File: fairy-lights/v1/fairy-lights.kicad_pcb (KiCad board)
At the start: 2 copper layers, 60 x 40 mm, 14 parts, among them J1 Conn_01x03_Male, J2 Screw_Terminal_01x02, J3 Conn_01x02_Pin, Q1 BSS138, U1 WeMos_D1_mini

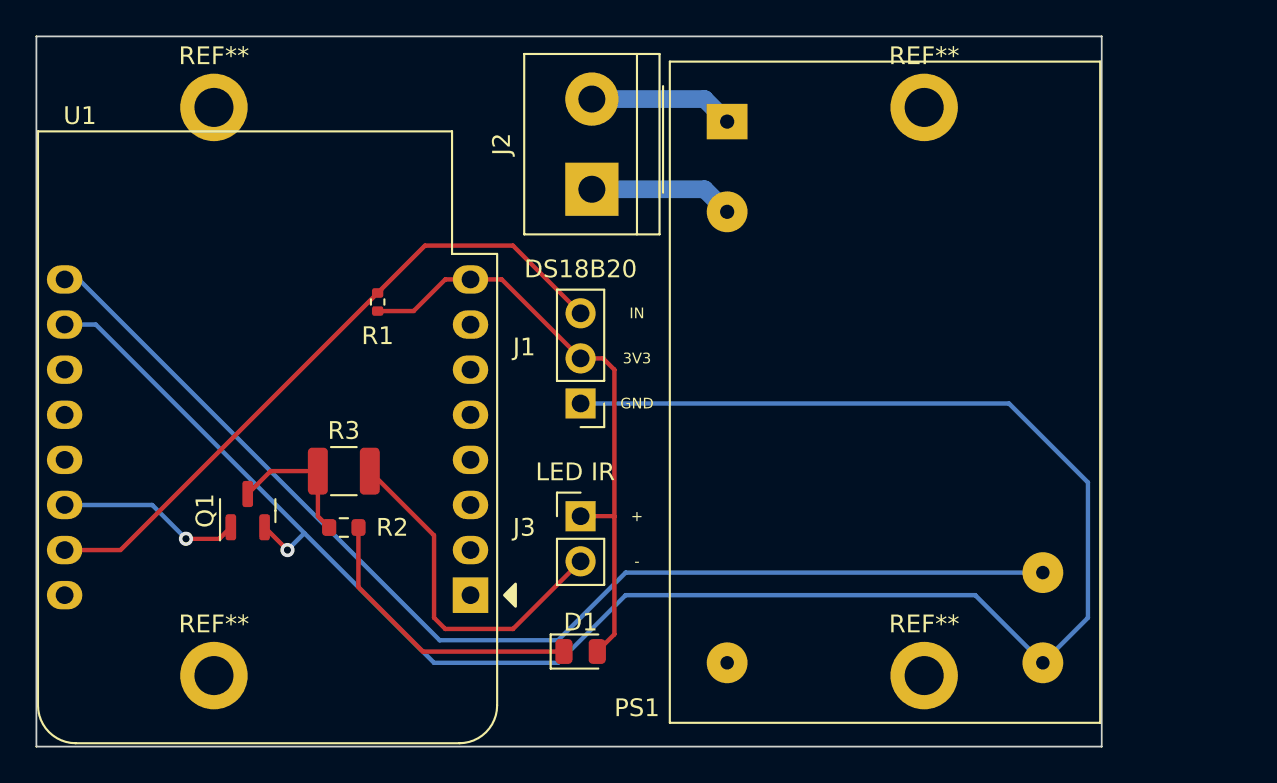
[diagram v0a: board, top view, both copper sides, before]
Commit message: finish schematic + footprints
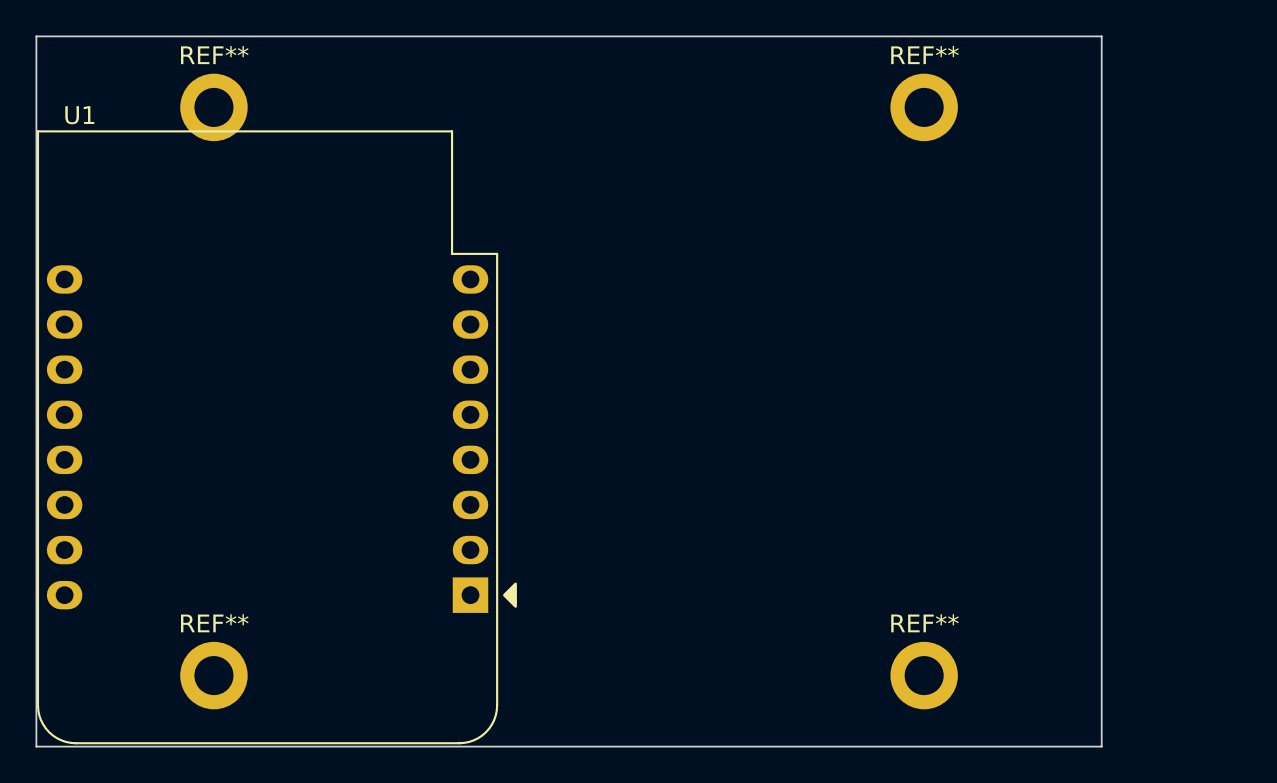
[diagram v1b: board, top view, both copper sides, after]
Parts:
- removed D1: LED, Diode_SMD:D_0805_2012Metric
- removed J1: Conn_01x03_Male, Connector_PinHeader_2.54mm:PinHeader_1x03_P2.54mm_Vertical
- removed J2: Screw_Terminal_01x02, TerminalBlock:TerminalBlock_bornier-2_P5.08mm
- removed J3: Conn_01x02_Pin, Connector_PinHeader_2.54mm:PinHeader_1x02_P2.54mm_Vertical
- removed PS1: Alim RS PRO 5V 1A, Converter_ACDC:Converter_ACDC_MeanWell_IRM-03-xx_THT
- removed Q1: BSS138, Package_TO_SOT_SMD:SOT-23
- removed R1: 4.7KΩ, Resistor_SMD:R_0402_1005Metric
- removed R2: 1KΩ, Resistor_SMD:R_0603_1608Metric
- removed R3: 18Ω/0.5W, Resistor_SMD:R_1210_3225Metric
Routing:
- net GND: track 110.9 -> 0.00 mm, vias 1 -> 0
- net +5V: track 65.1 -> 0.80 mm
- net Net-(J1-Pin_3): track 37.7 -> 0.00 mm
- net +3V3: track 34.4 -> 0.00 mm
- net Net-(J3-Pin_2): track 19.8 -> 0.00 mm
- net Net-(D1-K): track 16.4 -> 0.00 mm
- net Net-(Q1-G): track 10.4 -> 0.00 mm, vias 1 -> 0
- net NEUT: track 8.15 -> 0.00 mm
- net LINE: track 8.15 -> 0.00 mm
- net Net-(Q1-D): track 7.92 -> 0.00 mm
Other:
- board text removed: "+"
- board text removed: "-"
- board text removed: "3V3"
- board text removed: "DS18B20"
- board text removed: "GND"
- board text removed: "IN"
- board text removed: "LED IR"

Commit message: placement
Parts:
- added HS1: Heatsink, Heatsink:Heatsink_Fischer_SK104-STC-STIC_35x13mm_2xDrill2.5mm, F.Cu at (124.8, 67.3)
- added J2: Screw_Terminal_01x02, TerminalBlock:TerminalBlock_bornier-2_P5.08mm, F.Cu at (139.1, 69.8)
- added J4: Screw_Terminal_01x03, TerminalBlock:TerminalBlock_bornier-3_P5.08mm, F.Cu at (146.7, 59.7)
- added Q1: IRLZ44N, Package_TO_SOT_THT:TO-220-3_Vertical, F.Cu at (121.3, 64.8)
- added R1: 10KΩ, Resistor_THT:R_Axial_DIN0207_L6.3mm_D2.5mm_P15.24mm_Horizontal, F.Cu at (95.9, 54.6)
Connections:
- U1 pad 8: +3V3 -> unconnected-(U1-3V3-Pad8)

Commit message: wip routing
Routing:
- net GND: track 0.00 -> 72.8 mm
- net Net-(J4-Pin_3): track 0.00 -> 18.4 mm
- net +5V: track 0.80 -> 14.1 mm
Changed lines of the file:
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@@
   (gr_rect locked (start 90 46) (end 150 86)
     (stroke (width 0.1) (type default)) (fill none) (layer "Edge.Cuts"))
+  (segment (start 128.905 74.93) (end 123.825 69.85) (width 1) (layer "B.Cu") (net 1))
+  (segment (start 139.065 74.93) (end 128.905 74.93) (width 1) (layer "B.Cu") (net 1))
+  (segment (start 118.745 80.01) (end 109.37 80.01) (width 0.25) (layer "B.Cu") (net 1))
+  (segment (start 109.37 80.01) (end 91.59 62.23) (width 0.25) (layer "B.Cu") (net 1))
+  (segment (start 121.285 77.47) (end 118.745 80.01) (width 0.25) (layer "B.Cu") (net 1))
+  (segment (start 123.825 69.85) (end 121.285 69.85) (width 1) (layer "B.Cu") (net 1))
+  (segment (start 144.145 69.85) (end 139.065 74.93) (width 1) (layer "B.Cu") (net 1))
+  (segment (start 121.285 69.85) (end 121.285 77.47) (width 0.25) (layer "B.Cu") (net 1))
+  (segment (start 146.685 59.69) (end 139.065 67.31) (width 1) (layer "B.Cu") (net 2))
   (segment (start 92.3925 59.69) (end 91.59 59.69) (width 0.25) (layer "B.Cu") (net 2))
+  (segment (start 139.065 67.31) (end 139.065 69.85) (width 1) (layer "B.Cu") (net 2))
+  (segment (start 121.285 67.31) (end 128.905 67.31) (width 1) (layer "B.Cu") (net 16))
+  (segment (start 128.905 67.31) (end 136.525 59.69) (width 1) (layer "B.Cu") (net 16))
   (group "" (id d3af2464-7c72-4396-9bd6-7c833b8b6ea2)
     (members

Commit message: routing
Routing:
- net +5V: track 14.1 -> 76.8 mm
- net Net-(J4-Pin_2): track 0.00 -> 62.6 mm
- net Net-(Q1-G): track 0.00 -> 49.6 mm
- net GND: track 72.8 -> 92.9 mm
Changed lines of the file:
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@@
   (gr_rect locked (start 90 46) (end 150 86)
     (stroke (width 0.1) (type default)) (fill none) (layer "Edge.Cuts"))
+  (segment (start 111.125 54.61) (end 112.25637 54.61) (width 0.25) (layer "B.Cu") (net 1))
+  (segment (start 118.745 67.31) (end 121.285 69.85) (width 0.25) (layer "B.Cu") (net 1))
   (segment (start 128.905 74.93) (end 123.825 69.85) (width 1) (layer "B.Cu") (net 1))
   (segment (start 139.065 74.93) (end 128.905 74.93) (width 1) (layer "B.Cu") (net 1))
@@
   (segment (start 109.37 80.01) (end 91.59 62.23) (width 0.25) (layer "B.Cu") (net 1))
   (segment (start 121.285 77.47) (end 118.745 80.01) (width 0.25) (layer "B.Cu") (net 1))
+  (segment (start 112.25637 54.61) (end 118.745 61.09863) (width 0.25) (layer "B.Cu") (net 1))
   (segment (start 123.825 69.85) (end 121.285 69.85) (width 1) (layer "B.Cu") (net 1))
   (segment (start 144.145 69.85) (end 139.065 74.93) (width 1) (layer "B.Cu") (net 1))
+  (segment (start 118.745 61.09863) (end 118.745 67.31) (width 0.25) (layer "B.Cu") (net 1))
   (segment (start 121.285 69.85) (end 121.285 77.47) (width 0.25) (layer "B.Cu") (net 1))
   (segment (start 146.685 59.69) (end 139.065 67.31) (width 1) (layer "B.Cu") (net 2))
-  (segment (start 92.3925 59.69) (end 91.59 59.69) (width 0.25) (layer "B.Cu") (net 2))
+  (segment (start 100.965 59.69) (end 111.125 49.53) (width 0.25) (layer "B.Cu") (net 2))
+  (segment (start 141.605 54.61) (end 146.685 59.69) (width 0.25) (layer "B.Cu") (net 2))
+  (segment (start 111.125 49.53) (end 133.985 49.53) (width 0.25) (layer "B.Cu") (net 2))
+  (segment (start 91.59 59.69) (end 100.965 59.69) (width 0.25) (layer "B.Cu") (net 2))
+  (segment (start 139.065 54.61) (end 141.605 54.61) (width 0.25) (layer "B.Cu") (net 2))
+  (segment (start 133.985 49.53) (end 139.065 54.61) (width 0.25) (layer "B.Cu") (net 2))
   (segment (start 139.065 67.31) (end 139.065 69.85) (width 1) (layer "B.Cu") (net 2))
+  (segment (start 95.885 68.095) (end 95.885 54.61) (width 0.25) (layer "F.Cu") (net 3))
+  (segment (start 121.285 64.77) (end 121.285 62.23) (width 0.25) (layer "F.Cu") (net 3))
+  (segment (start 91.59 72.39) (end 95.885 68.095) (width 0.25) (layer "F.Cu") (net 3))
+  (segment (start 121.285 62.23) (end 116.205 57.15) (width 0.25) (layer "F.Cu") (net 3))
+  (segment (start 116.205 57.15) (end 95.885 57.15) (width 0.25) (layer "F.Cu") (net 3))
+  (segment (start 108.585 82.55) (end 113.665 82.55) (width 0.25) (layer "F.Cu") (net 15))
+  (segment (start 113.665 82.55) (end 133.985 62.23) (width 0.25) (layer "F.Cu") (net 15))
+  (segment (start 91.59 74.93) (end 100.965 74.93) (width 0.25) (layer "F.Cu") (net 15))
+  (segment (start 100.965 74.93) (end 108.585 82.55) (width 0.25) (layer "F.Cu") (net 15))
+  (segment (start 139.065 62.23) (end 141.605 59.69) (width 0.25) (layer "F.Cu") (net 15))
+  (segment (start 133.985 62.23) (end 139.065 62.23) (width 0.25) (layer "F.Cu") (net 15))
   (segment (start 121.285 67.31) (end 128.905 67.31) (width 1) (layer "B.Cu") (net 16))
   (segment (start 128.905 67.31) (end 136.525 59.69) (width 1) (layer "B.Cu") (net 16))

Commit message: routing + sign
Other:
- board text added: "Éléonore et Papa"

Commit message: wiring
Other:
- board text added: "+"
- board text added: "-"
- board text added: ". +"
- board text added: "D"
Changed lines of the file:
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@@
     (property "ki_keywords" "screw terminal")
     (attr through_hole)
-    (fp_text reference "J4" (at 2.54 5.08) (layer "F.SilkS")
+    (fp_text reference "J4" (at 13.97 1.27) (layer "F.SilkS")
         (effects (font (size 1 1) (thickness 0.15)))
     )
@@
   (gr_rect locked (start 90 46) (end 150 86)
     (stroke (width 0.1) (type default)) (fill none) (layer "Edge.Cuts"))
+  (gr_text " .\n+" (at 145.415 55.88) (layer "F.SilkS")
+    (effects (font (size 1.5 1.5) (thickness 0.3) bold) (justify left bottom))
+  )
+  (gr_text "D" (at 140.335 55.88) (layer "F.SilkS")
+    (effects (font (size 1.5 1.5) (thickness 0.3) bold) (justify left bottom))
+  )
+  (gr_text "-" (at 142.875 75.565) (layer "F.SilkS")
+    (effects (font (size 1.5 1.5) (thickness 0.3) bold) (justify left bottom))
+  )
+  (gr_text "+" (at 137.795 75.565) (layer "F.SilkS")
+    (effects (font (size 1.5 1.5) (thickness 0.3) bold) (justify left bottom))
+  )
+  (gr_text "-" (at 135.255 55.88) (layer "F.SilkS")
+    (effects (font (size 1.5 1.5) (thickness 0.3) bold) (justify left bottom))
+  )
   (gr_text "Éléonore et Papa" (at 132.08 77.47) (layer "F.SilkS")
     (effects (font (face "Comic Sans MS") (size 1.5 1.5) (thickness 0.3) bold) (justify left bottom))
